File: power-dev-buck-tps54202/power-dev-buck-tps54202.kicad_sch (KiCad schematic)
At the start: 0 parts

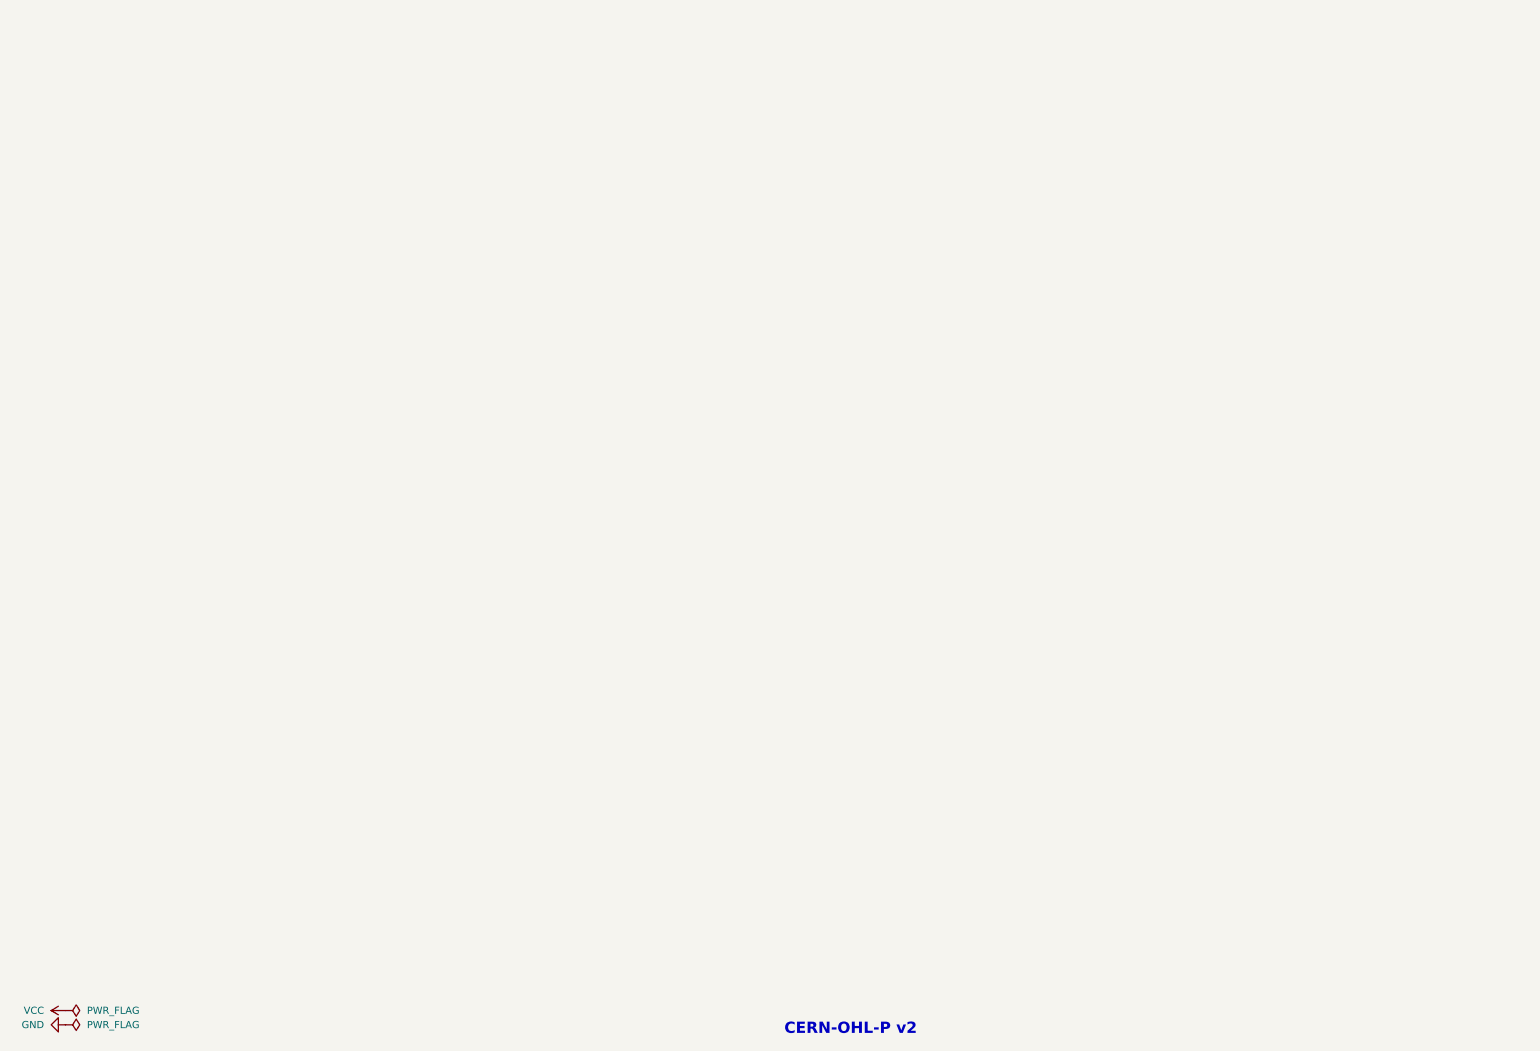
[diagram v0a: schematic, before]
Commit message: Implement power-dev-buck-tps54202
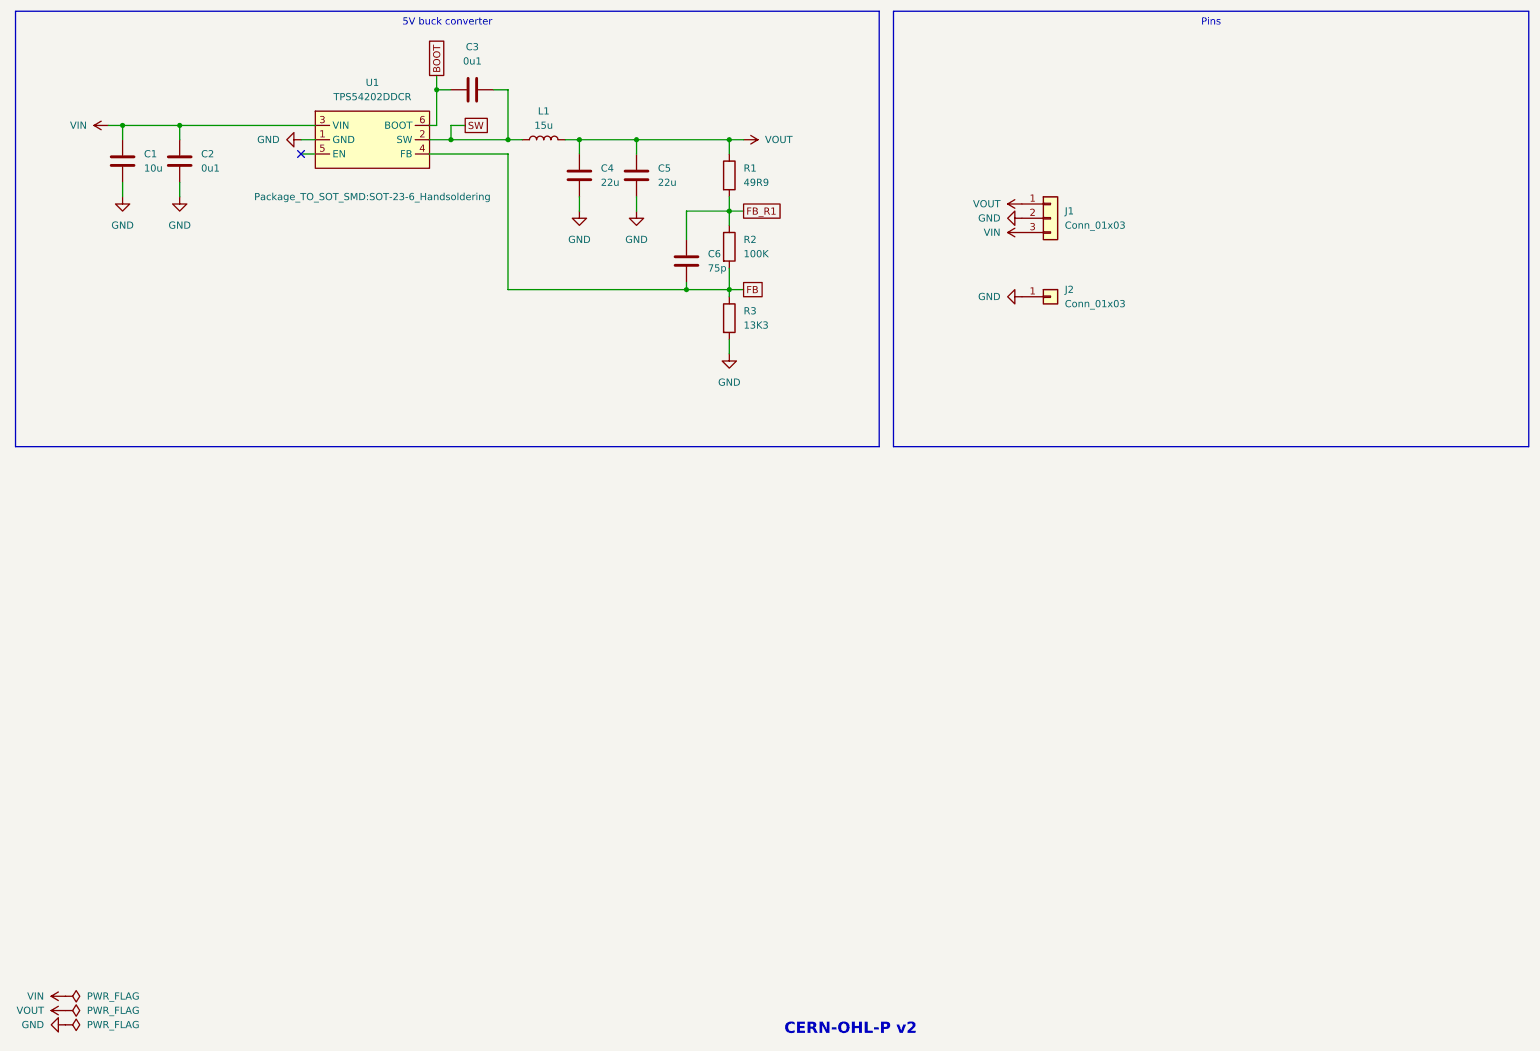
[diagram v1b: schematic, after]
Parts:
- added C1: 10u, custom:C_0805_2012Metric_Pad1.18x1.45mm_HandSolder, symbol Device:C
- added C2, C3: 0u1, custom:C_0805_2012Metric_Pad1.18x1.45mm_HandSolder, symbol Device:C
- added C4, C5: 22u, custom:C_0805_2012Metric_Pad1.18x1.45mm_HandSolder, symbol Device:C
- added C6: 75p, custom:C_0805_2012Metric_Pad1.18x1.45mm_HandSolder, symbol Device:C
- added J1: Conn_01x03, custom:PinHeader_1x03_P2.54mm_Vertical_simple_pad2gnd, symbol Connector_Generic:Conn_01x03
- added J2: Conn_01x03, custom:PinHeader_1x01_P2.54mm_simple_square, symbol Connector_Generic:Conn_01x01
- added L1: 15u, custom:Inductor_Multi_5.2x5.7_2x2.5, symbol Device:L
- added R1: 49R9, Resistor_SMD:R_0805_2012Metric_Pad1.20x1.40mm_HandSolder, symbol Device:R
- added R2: 100K, Resistor_SMD:R_0805_2012Metric_Pad1.20x1.40mm_HandSolder, symbol Device:R
- added R3: 13K3, Resistor_SMD:R_0805_2012Metric_Pad1.20x1.40mm_HandSolder, symbol Device:R
- added U1: TPS54202DDCR, Package_TO_SOT_SMD:SOT-23-6_Handsoldering, symbol lcsc:TPS54202DDCR
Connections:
- net GND: now also C1.2, C2.2, C4.2, C5.2, J1.2 (Pin_2), J2.1 (Pin_1), R3.2, U1.1 (GND)
- new net BOOT: C3.1, U1.6 (BOOT)
- new net FB: C6.2, R2.2, R3.1, U1.4 (FB)
- new net FB_R1: C6.1, R1.2, R2.1
- new net SW: C3.2, L1.1, U1.2 (SW)
- new net VIN: C1.1, C2.1, J1.3 (Pin_3), U1.3 (VIN)
- new net VOUT: C4.1, C5.1, J1.1 (Pin_1), L1.2, R1.1
- no-connect marks 0 -> 1
